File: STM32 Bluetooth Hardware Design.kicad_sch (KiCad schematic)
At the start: 11 parts, among them U1 STM32WB55CEUx

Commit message: First commit
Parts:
- added C11: C, symbol Device:C
- added L1: 10n, symbol Device:L
- added L2: 10u, symbol Device:L
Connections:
- net GND: now also C11.2
- net at U1.31 (VFBSMPS): now also C11.1, L2.2
- net SMPSLX: now reaches U1.33 (VLXSMPS)
- net SMPSLX: now also L1.1, L1.2, L2.1

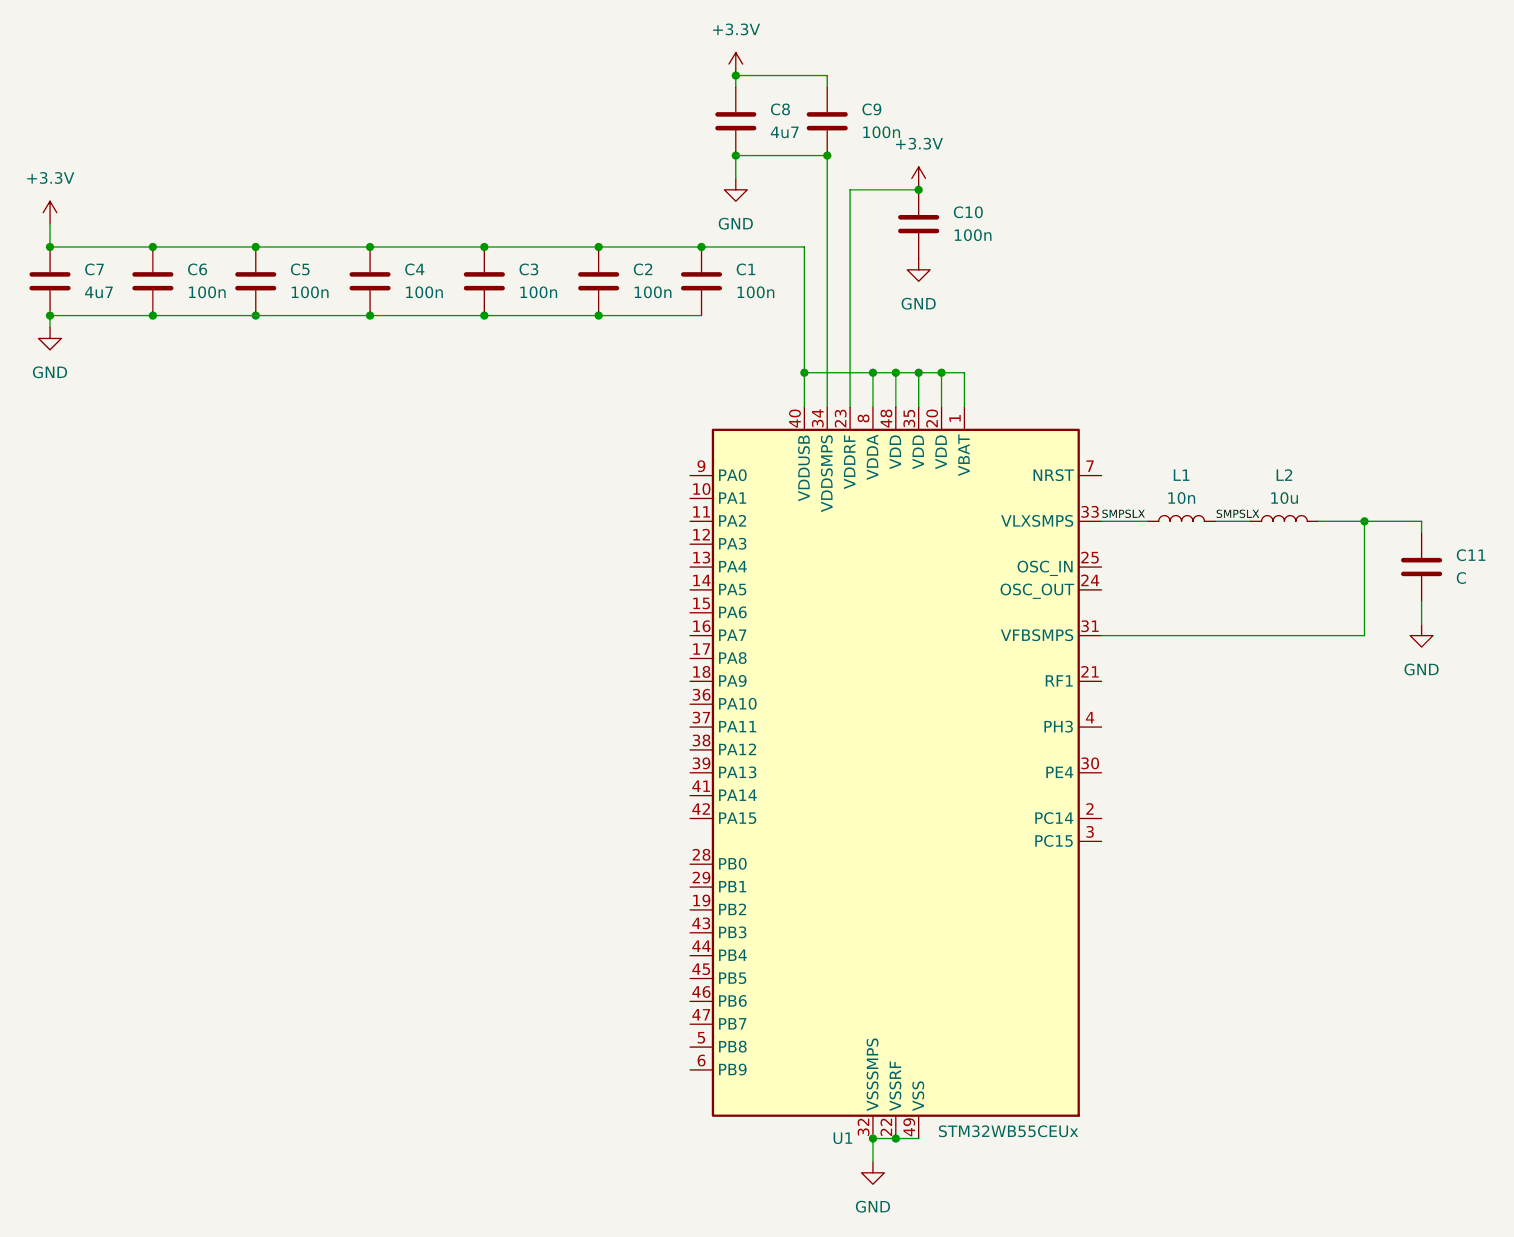
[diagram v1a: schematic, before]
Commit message: added schematic sections and stm32cube file
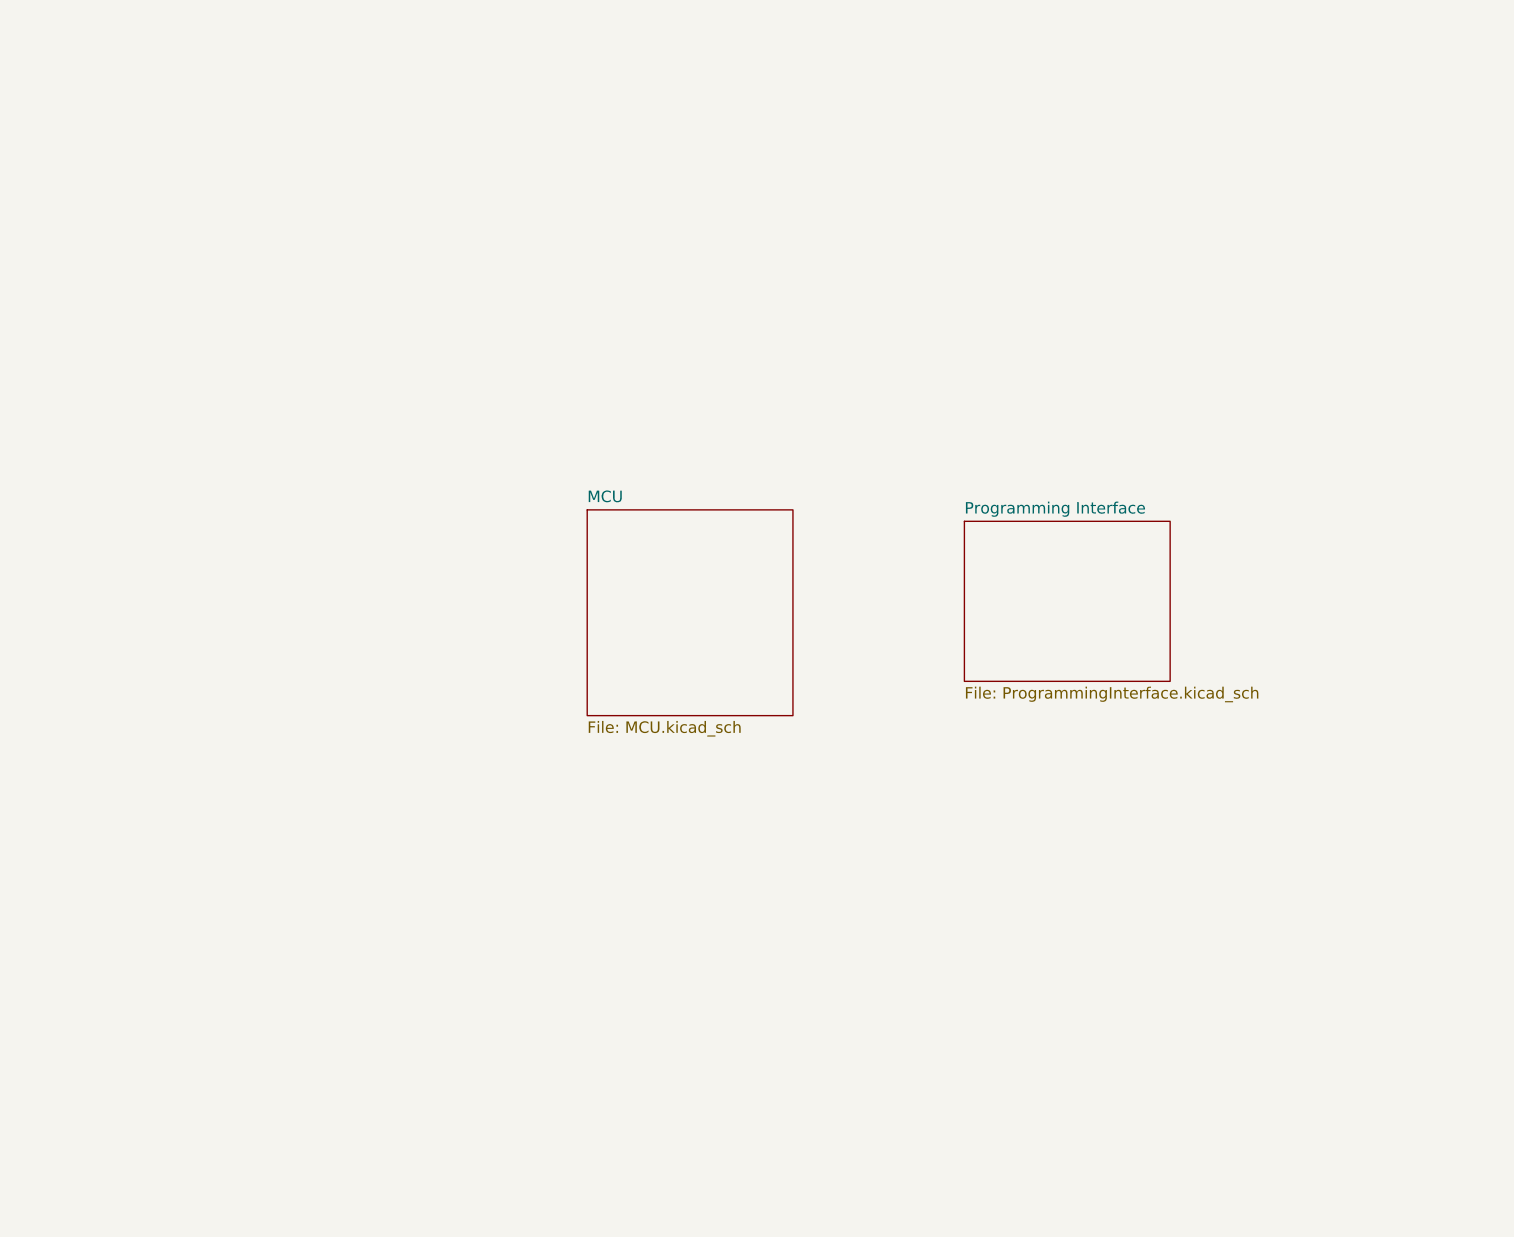
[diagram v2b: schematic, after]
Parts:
- removed C1, C10, C2, C3, C4, C5, C6, C9: 100n, symbol Device:C
- removed C11: C, symbol Device:C
- removed C7, C8: 4u7, symbol Device:C
- removed L1: 10n, symbol Device:L
- removed L2: 10u, symbol Device:L
- removed U1: STM32WB55CEUx, Package_DFN_QFN:QFN-48-1EP_7x7mm_P0.5mm_EP5.6x5.6mm, symbol MCU_ST_STM32WB:STM32WB55CEUx
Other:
- added sheet MCU (MCU.kicad_sch)
- added sheet Programming Interface (ProgrammingInterface.kicad_sch)

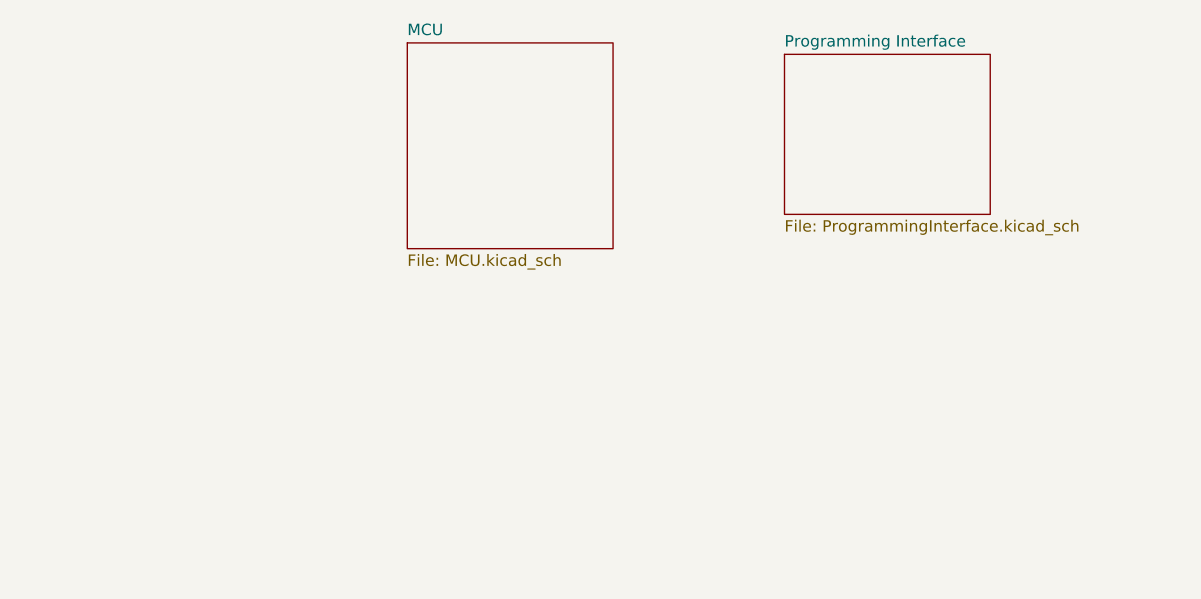
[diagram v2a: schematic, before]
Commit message: finished rf section, added usb, and power sections
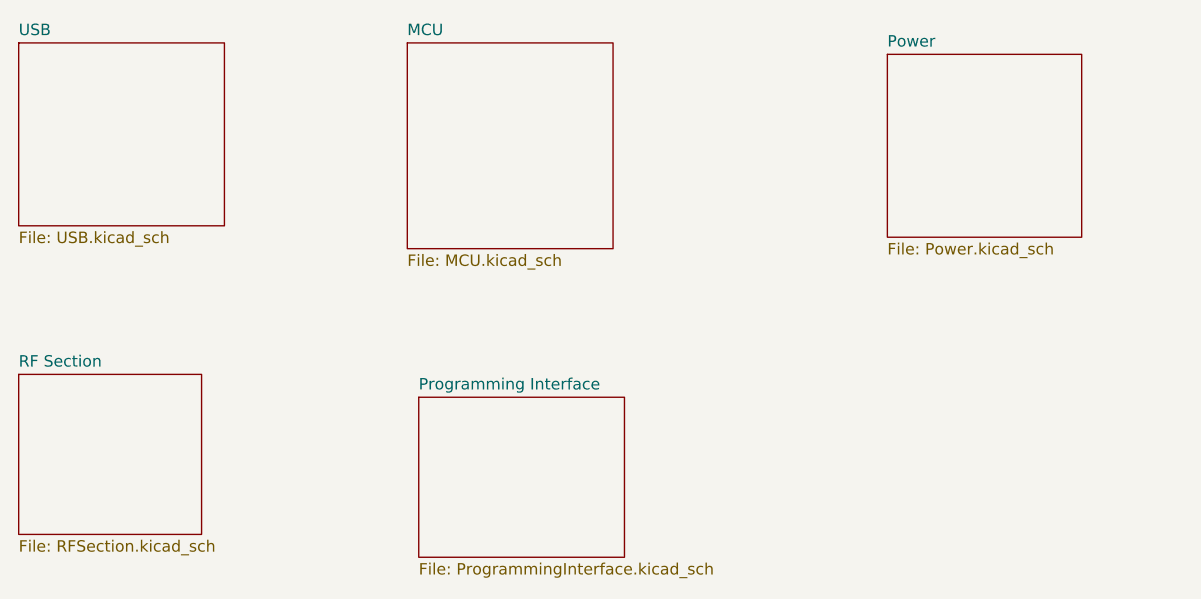
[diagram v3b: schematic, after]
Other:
- added sheet Power (Power.kicad_sch)
- added sheet RF Section (RFSection.kicad_sch)
- added sheet USB (USB.kicad_sch)
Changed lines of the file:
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@@
 	(paper "A4")
 	(sheet
-		(at 170.18 80.01)
+		(at 85.09 78.74)
+		(size 22.86 20.32)
+		(exclude_from_sim no)
+		(in_bom yes)
+		(on_board yes)
+		(dnp no)
+		(fields_autoplaced yes)
+		(stroke
+			(width 0.1524)
+			(type solid)
+		)
+		(fill
+			(color 0 0 0 0.0000)
+		)
+		(property "Sheetname" "USB"
+			(at 85.09 78.0284 0)
+			(effects
+				(font
+					(size 1.27 1.27)
+				)
+				(justify left bottom)
+			)
+		)
+		(property "Sheetfile" "USB.kicad_sch"
+			(at 85.09 99.6446 0)
+			(effects
+				(font
+					(size 1.27 1.27)
+				)
+				(justify left top)
+			)
+		)
+		(instances
+			(project "STM32 Bluetooth Hardware Design"
+				(path "/7294b0c1-22f8-4dfa-8bae-2337522835ff"
+					(page "5")
+				)
+			)
+		)
+	)
+	(sheet
+		(at 85.09 115.57)
+		(size 20.32 17.78)
+		(exclude_from_sim no)
+		(in_bom yes)
+		(on_board yes)
+		(dnp no)
+		(fields_autoplaced yes)
+		(stroke
+			(width 0.1524)
+			(type solid)
+		)
+		(fill
+			(color 0 0 0 0.0000)
+		)
+		(property "Sheetname" "RF Section"
+			(at 85.09 114.8584 0)
+			(effects
+				(font
+					(size 1.27 1.27)
+				)
+				(justify left bottom)
+			)
+		)
+		(property "Sheetfile" "RFSection.kicad_sch"
+			(at 85.09 133.9346 0)
+			(effects
+				(font
+					(size 1.27 1.27)
+				)
+				(justify left top)
+			)
+		)
+		(instances
+			(project "STM32 Bluetooth Hardware Design"
+				(path "/7294b0c1-22f8-4dfa-8bae-2337522835ff"
+					(page "4")
+				)
+			)
+		)
+	)
+	(sheet
+		(at 129.54 118.11)
 		(size 22.86 17.78)
 		(exclude_from_sim no)
@@
 		)
 		(property "Sheetname" "Programming Interface"
-			(at 170.18 79.2984 0)
+			(at 129.54 117.3984 0)
 			(effects
 				(font
@@
 		)
 		(property "Sheetfile" "ProgrammingInterface.kicad_sch"
-			(at 170.18 98.3746 0)
+			(at 129.54 136.4746 0)
 			(effects
 				(font
@@
 				)
 			)
+		)
+	)
+	(sheet
+		(at 181.61 80.01)
+		(size 21.59 20.32)
+		(exclude_from_sim no)
+		(in_bom yes)
+		(on_board yes)
+		(dnp no)
+		(fields_autoplaced yes)
+		(stroke
+			(width 0.1524)
+			(type solid)
+		)
+		(fill
+			(color 0 0 0 0.0000)
+		)
+		(property "Sheetname" "Power"
+			(at 181.61 79.2984 0)
+			(effects
+				(font
+					(size 1.27 1.27)
+				)
+				(justify left bottom)
+			)
+		)
+		(property "Sheetfile" "Power.kicad_sch"
+			(at 181.61 100.9146 0)
+			(effects
+				(font
+					(size 1.27 1.27)
+				)
+				(justify left top)
+			)
+		)
+		(instances
+			(project "STM32 Bluetooth Hardware Design"
+				(path "/7294b0c1-22f8-4dfa-8bae-2337522835ff"
+					(page "6")
+				)
+			)

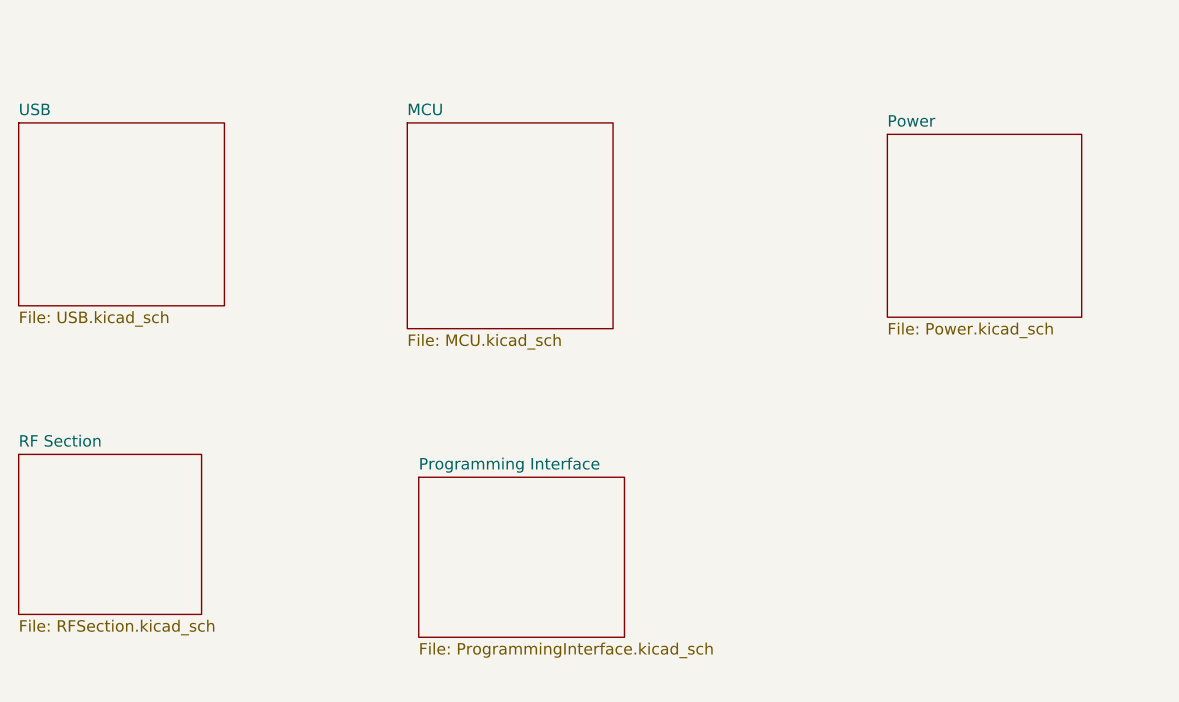
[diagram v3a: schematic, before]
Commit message: fixed some nets
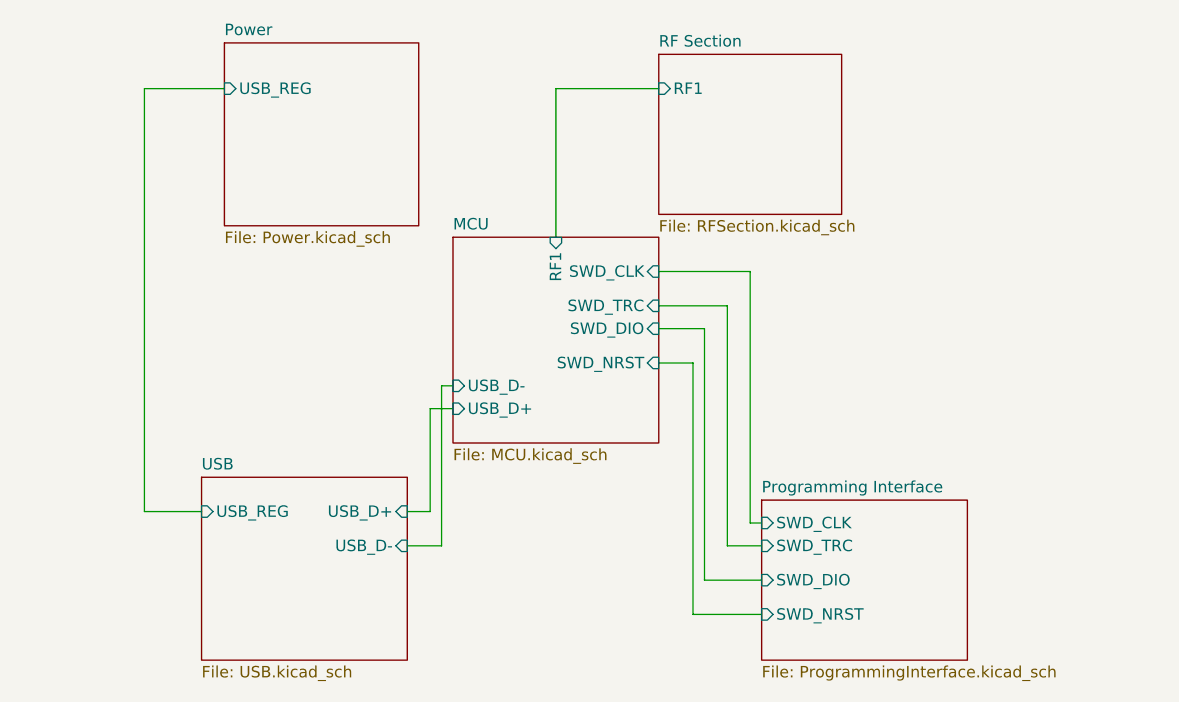
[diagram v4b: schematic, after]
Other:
- sheet MCU ports: added RF1, SWD_CLK, SWD_DIO, SWD_NRST, SWD_TRC, USB_D+, USB_D-; removed none
- sheet Power ports: added USB_REG; removed none
- sheet Programming Interface ports: added SWD_CLK, SWD_DIO, SWD_NRST, SWD_TRC; removed none
- sheet RF Section ports: added RF1; removed none
- sheet USB ports: added USB_D+, USB_D-, USB_REG; removed none
